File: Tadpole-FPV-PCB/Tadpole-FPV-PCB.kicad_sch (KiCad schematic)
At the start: 19 parts, among them J1 U1 Debug, J2 U2 Debug, J3 Left Gimbal, J4 Right Gimbal, P1 USB_C_Plug_USB2.0, SW1 Power Switch, SW2 Left Switch, SW3 Right Switch, U1 ESP32-WROOM-32, U2 ESP32-WROOM-32, U3 E28-2G4M27S

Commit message: Finished PCB Schematic Design (Again)
I feel like this might happen a couple more times...
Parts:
- removed U4: ~, Connector_PinHeader_2.54mm:PinHeader_1x04_P2.54mm_Vertical, symbol Custom:DC-DC_Step_Down
- added C2, C3: 22uF, Capacitor_SMD:C_0603_1608Metric, symbol Device:C
- added D2: LED, Diode_SMD:D_0201_0603Metric, symbol Device:LED
- added L1: 470nH, Custom:IND-SMD_L4.0-W4.0_XGL4020, symbol Device:L
- added R3: 100, Resistor_SMD:R_0603_1608Metric, symbol Device:R
- added R4: 5.1k, Resistor_SMD:R_0603_1608Metric, symbol Device:R
- added R5: 100k, Resistor_SMD:R_0402_1005Metric, symbol Device:R
- added R6: 511k, Resistor_SMD:R_0402_1005Metric, symbol Device:R
- added R7: 91k, Resistor_SMD:R_0603_1608Metric, symbol Device:R
- added U4: ~, Custom:VSON-10_L3.0-W2.0-P0.50-TL, symbol Custom:TPS63802DLAR
- R1, R2: footprint Resistor_THT:R_Axial_DIN0207_L6.3mm_D2.5mm_P7.62mm_Horizontal -> Resistor_SMD:R_0603_1608Metric
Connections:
- net +3.3V: now also C3.1, R5.1, R6.2, U4.6 (VOUT)
- net Battery +: now also BT2.2
- net GND: now also BT1.1, C2.1, C3.2, R7.1, U4.2 (MODE), U4.3 (AGND), U4.8 (GND)
- net GNDA: now also D2.1 (K), R4.2
- net VBUS: now reaches P1.A4 (VBUS), P1.A9 (VBUS), P1.B4 (VBUS), P1.B9 (VBUS), U5.1 (VIN+)
- net VBUS: now also R3.2
- net at P1.A5 (CC): now also P1.B5 (VCONN), R4.1
- net VIN: now reaches SW1.2 (B)
- net VIN: now also C2.2, U4.1 (EN), U4.10 (VIN)
- new net: R5.2, U4.5 (PG)
- new net: D2.2 (A), R3.1
- new net FB: R6.1, R7.2, U4.4 (FB)
- new net L1: L1.1, U4.9 (L1)
- new net L2: L1.2, U4.7 (L2)
- no-connect marks 45 -> 43
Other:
- moved on the sheet: BT1, BT2, C1, SW1A, U5

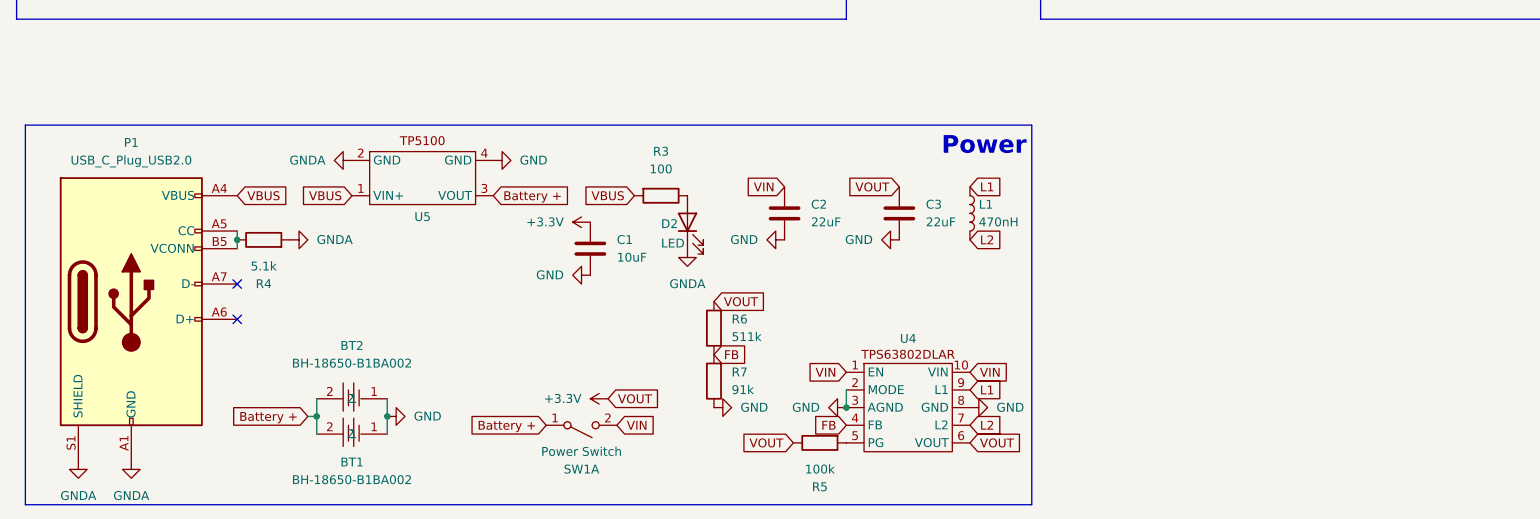
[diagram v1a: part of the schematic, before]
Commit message: Finished PCB Layout and Wiring + PCB Art!
Also fixed some layout issues from earlier Journal entries.
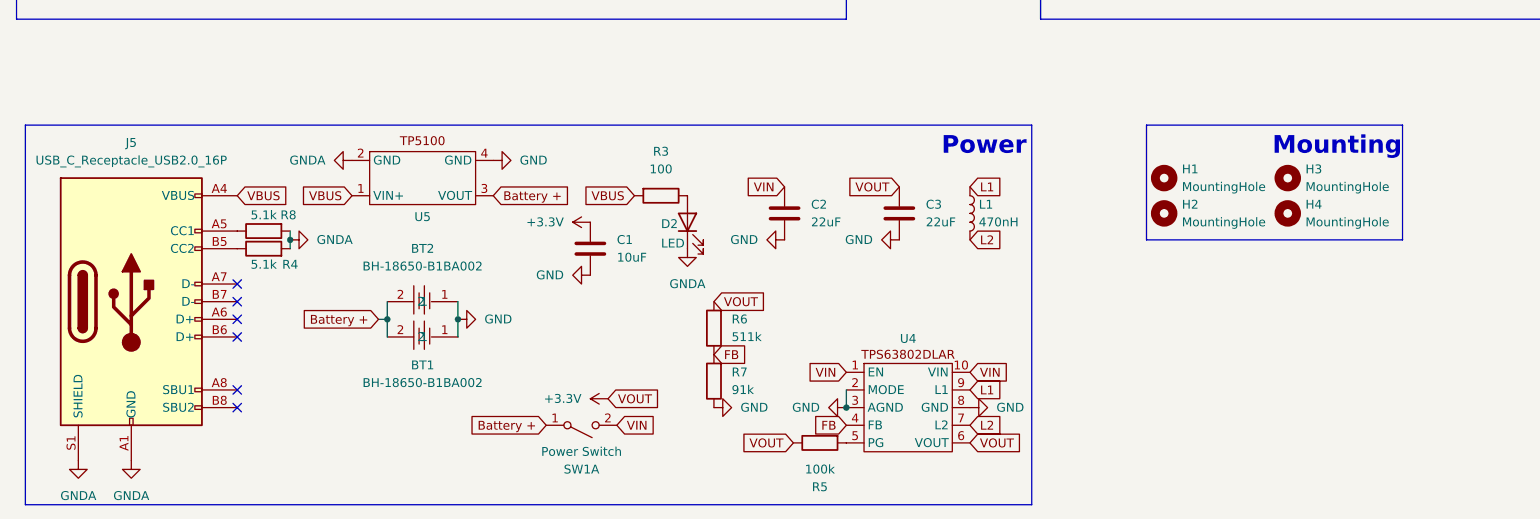
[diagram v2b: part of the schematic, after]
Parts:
- removed P1: USB_C_Plug_USB2.0, Connector_USB:USB_C_Receptacle_GCT_USB4105-xx-A_16P_TopMnt_Horizontal, symbol Connector:USB_C_Plug_USB2.0
- added H1, H2, H3, H4: MountingHole, MountingHole:MountingHole_3.2mm_M3_Pad_Via, symbol Mechanical:MountingHole
- added J5: USB_C_Receptacle_USB2.0_16P, Connector_USB:USB_C_Receptacle_GCT_USB4105-xx-A_16P_TopMnt_Horizontal, symbol Connector:USB_C_Receptacle_USB2.0_16P
- added R8: 5.1k, Resistor_SMD:R_0603_1608Metric, symbol Device:R
- D2: footprint Diode_SMD:D_0201_0603Metric -> Custom:0603 LED
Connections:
- net GNDA: now also J5.A1 (GND), J5.A12 (GND), J5.B1 (GND), J5.B12 (GND), J5.S1 (SHIELD), R8.2
- net VBUS: now also J5.A4 (VBUS), J5.A9 (VBUS), J5.B4 (VBUS), J5.B9 (VBUS)
- net at R4.1: now also J5.B5 (CC2)
- new net: J5.A5 (CC1), R8.1
- no-connect marks 43 -> 47
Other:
- note added: "Mounting"
- moved on the sheet: BT1, BT2, R4
